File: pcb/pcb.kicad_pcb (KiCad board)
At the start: 6 copper layers, 186 parts, among them J1201 Conn_02x07_Top_Bottom, J1401 FPGA_JTAG, J201 USB_B_Mini, J301 Conn_02x05_Top_Bottom, J302 1658525-9, J601 DB15_Female_HighDensity, J801 10067847-001RLF, J901 FTSH-110-01-L-DV-007, U1402 S25FL127SABMFV101, U201 TPS54325PWPR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

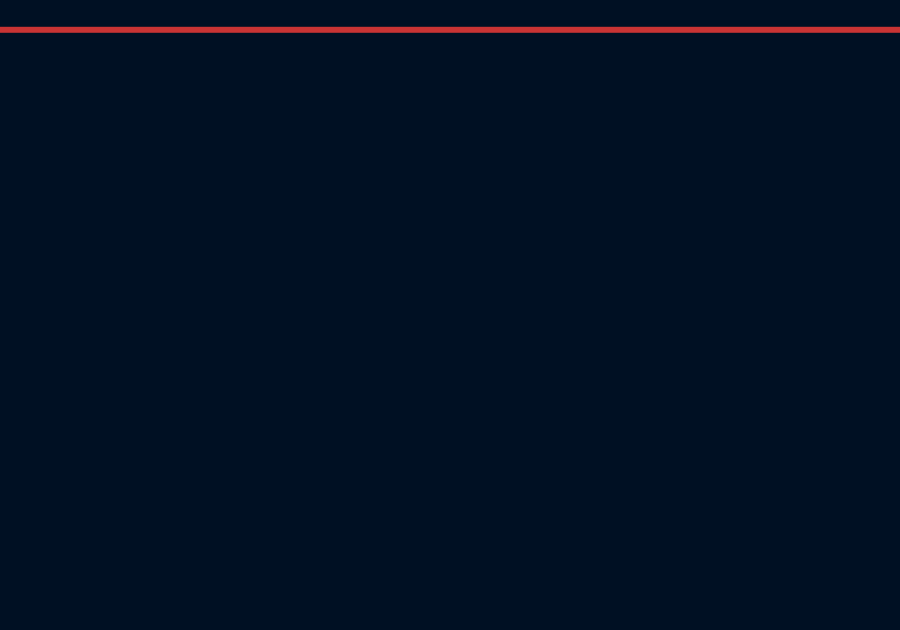
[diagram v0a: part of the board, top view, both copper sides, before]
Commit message: add correct vga resistors
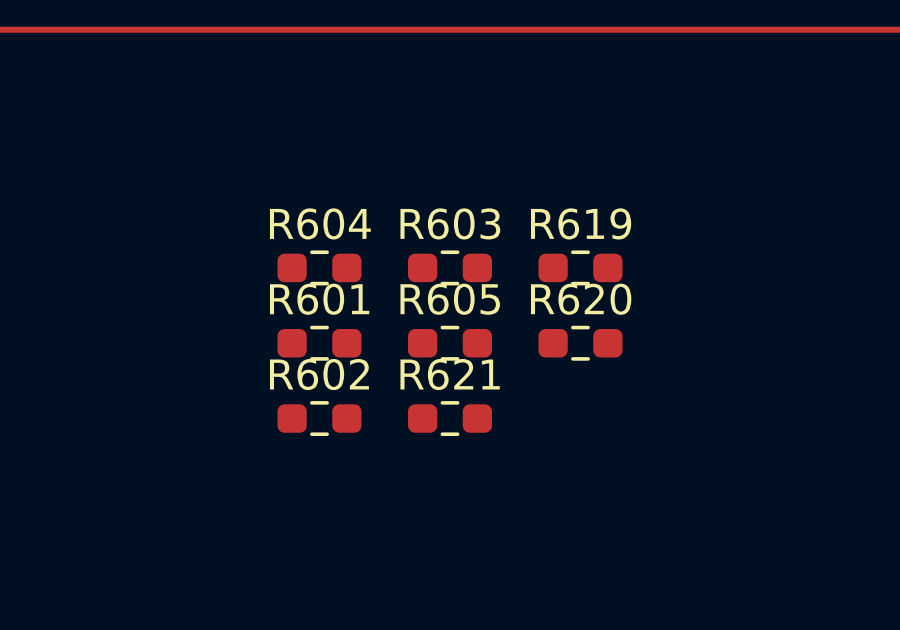
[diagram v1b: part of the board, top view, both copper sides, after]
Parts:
- added R601: 8760, Resistor_SMD:R_0603_1608Metric_Pad0.98x0.95mm_HandSolder, F.Cu at (141.5, 28.4)
- added R602: 4420, Resistor_SMD:R_0603_1608Metric_Pad0.98x0.95mm_HandSolder, F.Cu at (141.5, 31.0)
- added R603: 2200, Resistor_SMD:R_0603_1608Metric_Pad0.98x0.95mm_HandSolder, F.Cu at (145.8, 25.9)
- added R604: 1300, Resistor_SMD:R_0603_1608Metric_Pad0.98x0.95mm_HandSolder, F.Cu at (141.5, 25.9)
- added R605: 1100, Resistor_SMD:R_0603_1608Metric_Pad0.98x0.95mm_HandSolder, F.Cu at (145.8, 28.4)
- added R619: 1100, Resistor_SMD:R_0603_1608Metric_Pad0.98x0.95mm_HandSolder, F.Cu at (150.2, 25.9)
- added R620: 1100, Resistor_SMD:R_0603_1608Metric_Pad0.98x0.95mm_HandSolder, F.Cu at (150.2, 28.4)
- added R621: 1100, Resistor_SMD:R_0603_1608Metric_Pad0.98x0.95mm_HandSolder, F.Cu at (145.8, 31.0)
- R611, R616: value 550 -> 1100

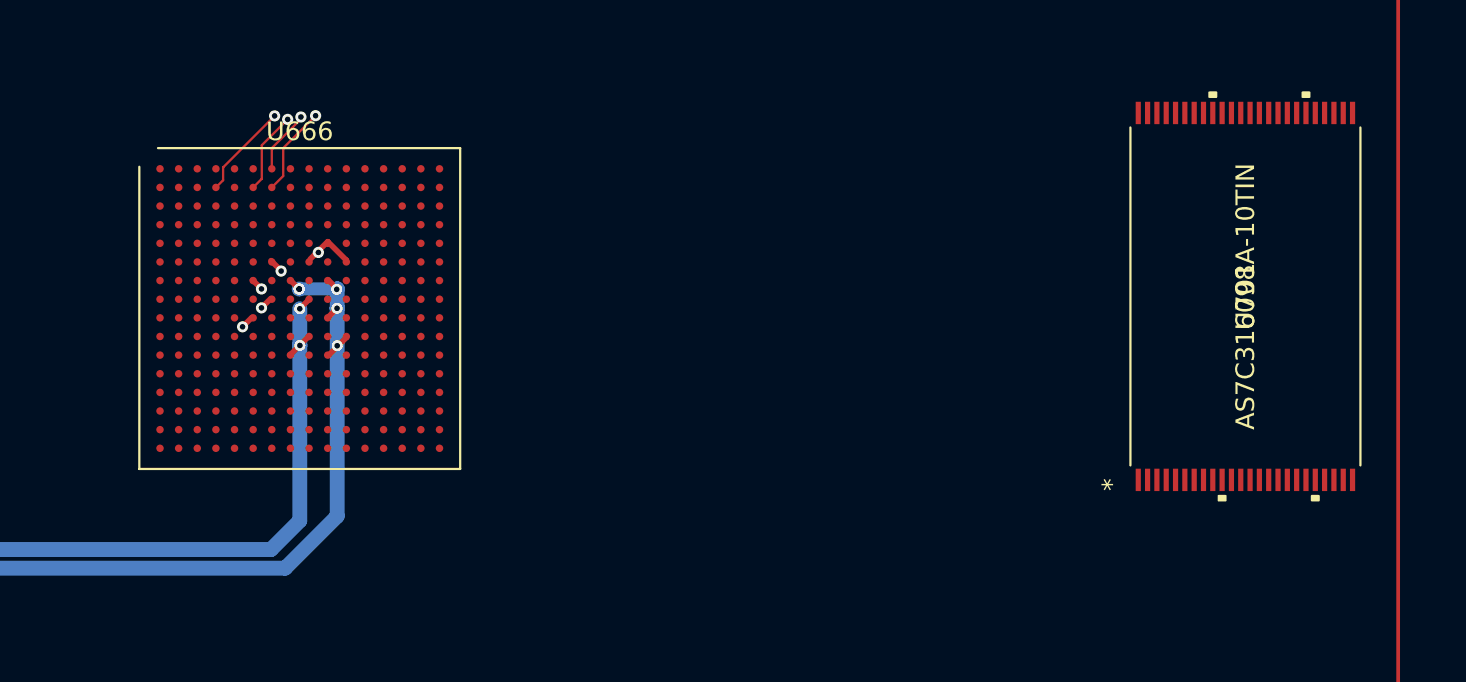
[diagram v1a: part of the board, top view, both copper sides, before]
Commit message: make lines between sram and fpga
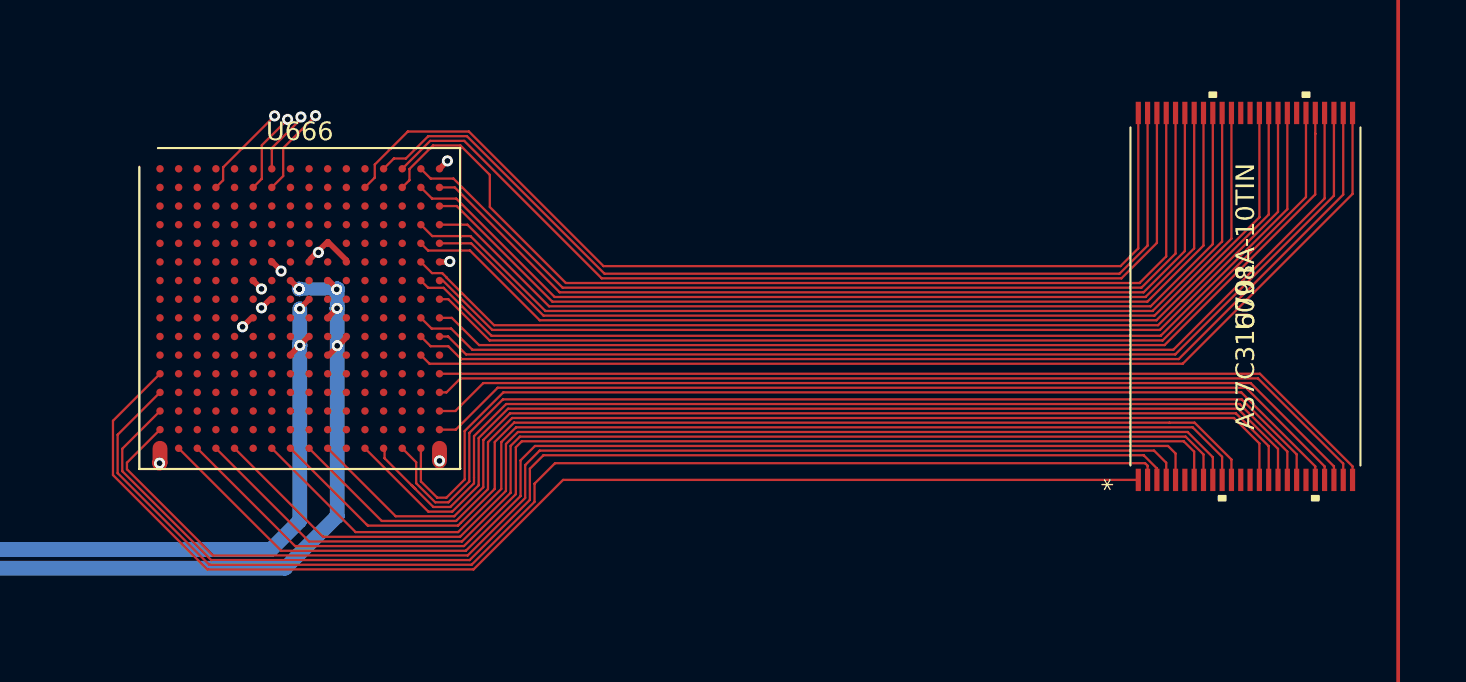
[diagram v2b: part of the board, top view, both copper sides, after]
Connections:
- U666 pad A13: vga_r2 -> SRAM_A6
- U666 pad A14: vga_r3 -> SRAM_A7
- U666 pad A15: vga_hsync -> SRAM_#OE
- U666 pad B12: vga_g4 -> SRAM_A5
- U666 pad B14: vga_r5 -> SRAM_A19
- U666 pad B15: unconnected-(U666-PadB15) -> SRAM_#LB
- U666 pad B16: unconnected-(U666-PadB16) -> SRAM_#UB
- U666 pad C16: vga_vsync -> SRAM_D15
- U666 pad D15: unconnected-(U666-PadD15) -> SRAM_D13
- U666 pad D16: unconnected-(U666-PadD16) -> SRAM_D14
- U666 pad E15: unconnected-(U666-PadE15) -> SRAM_D11
- U666 pad E16: unconnected-(U666-PadE16) -> SRAM_D12
- U666 pad F15: unconnected-(U666-PadF15) -> SRAM_D10
- U666 pad G15: unconnected-(U666-PadG15) -> SRAM_D8
- U666 pad G16: unconnected-(U666-PadG16) -> SRAM_D9
- U666 pad H16: unconnected-(U666-PadH16) -> SRAM_A8
- U666 pad J13: SRAM_A0 -> vga_r5
- U666 pad J14: SRAM_A1 -> unconnected-(U666-PadJ14)
- U666 pad J15: unconnected-(U666-PadJ15) -> SRAM_A10
- U666 pad J16: unconnected-(U666-PadJ16) -> SRAM_A9
- U666 pad K13: SRAM_A8 -> unconnected-(U666-PadK13)
- U666 pad K15: SRAM_A2 -> SRAM_A14
- U666 pad K16: SRAM_A3 -> SRAM_A11
- U666 pad L12: SRAM_A10 -> unconnected-(U666-PadL12)
- U666 pad L13: SRAM_A9 -> unconnected-(U666-PadL13)
- U666 pad L14: SRAM_A6 -> vga_r2
- U666 pad L15: SRAM_A4 -> SRAM_A16
- U666 pad M1: unconnected-(U666-PadM1) -> SRAM_A4
- U666 pad M12: SRAM_A11 -> unconnected-(U666-PadM12)
- U666 pad M14: SRAM_A7 -> vga_r3
- U666 pad M15: SRAM_A5 -> vga_g4
- U666 pad M6: SRAM_D14 -> unconnected-(U666-PadM6)
- U666 pad N1: unconnected-(U666-PadN1) -> SRAM_A3
- U666 pad N13: SRAM_D0 -> unconnected-(U666-PadN13)
- U666 pad N14: SRAM_D2 -> vga_hsync
- U666 pad N6: SRAM_D15 -> unconnected-(U666-PadN6)
- U666 pad N9: SRAM_D12 -> unconnected-(U666-PadN9)
- U666 pad P1: unconnected-(U666-PadP1) -> SRAM_A2
- U666 pad P10: SRAM_D4 -> unconnected-(U666-PadP10)
- U666 pad P11: SRAM_D5 -> unconnected-(U666-PadP11)
- U666 pad P13: SRAM_D1 -> unconnected-(U666-PadP13)
- U666 pad P14: SRAM_D3 -> unconnected-(U666-PadP14)
- U666 pad P15: SRAM_A14 -> unconnected-(U666-PadP15)
- U666 pad P8: SRAM_#CE -> unconnected-(U666-PadP8)
- U666 pad P9: SRAM_D13 -> vga_vsync
- U666 pad R1: unconnected-(U666-PadR1) -> SRAM_A1
- U666 pad R10: SRAM_D10 -> unconnected-(U666-PadR10)
- U666 pad R11: SRAM_D11 -> unconnected-(U666-PadR11)
- U666 pad R12: SRAM_D6 -> unconnected-(U666-PadR12)
- U666 pad R13: SRAM_D8 -> unconnected-(U666-PadR13)
- U666 pad R15: SRAM_A16 -> unconnected-(U666-PadR15)
- U666 pad R8: SRAM_#LB -> unconnected-(U666-PadR8)
- U666 pad T10: unconnected-(U666-PadT10) -> SRAM_D5
- U666 pad T12: SRAM_D7 -> SRAM_D6
- U666 pad T13: SRAM_D9 -> SRAM_D7
- U666 pad T14: SRAM_A18 -> SRAM_#WE
- U666 pad T15: SRAM_A19 -> SRAM_A0
- U666 pad T2: unconnected-(U666-PadT2) -> SRAM_A18
- U666 pad T3: unconnected-(U666-PadT3) -> SRAM_#CE
- U666 pad T4: unconnected-(U666-PadT4) -> SRAM_D0
- U666 pad T5: unconnected-(U666-PadT5) -> SRAM_D1
- U666 pad T7: SRAM_#OE -> SRAM_D2
- U666 pad T8: SRAM_#UB -> SRAM_D3
- U666 pad T9: SRAM_#WE -> SRAM_D4
- U701 pad 20: SRAM_A18 -> SRAM_A0
- U701 pad 22: SRAM_A16 -> SRAM_A15
- U701 pad 23: SRAM_A15 -> SRAM_A13
- U701 pad 24: SRAM_A14 -> SRAM_A12
- U701 pad 25: SRAM_A13 -> SRAM_A16
- U701 pad 26: SRAM_A12 -> SRAM_A14
- U701 pad 5: SRAM_A0 -> SRAM_A18
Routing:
- net SRAM_A3: track 0.00 -> 66.2 mm
- net SRAM_A2: track 0.00 -> 65.8 mm
- net SRAM_A4: track 0.00 -> 65.6 mm
- net SRAM_A1: track 0.00 -> 65.1 mm
- net SRAM_#CE: track 0.00 -> 61.2 mm
- net SRAM_A18: track 0.00 -> 60.8 mm
- net SRAM_D0: track 0.00 -> 60.6 mm
- net SRAM_D1: track 0.00 -> 60.1 mm
- net SRAM_D4: track 0.00 -> 58.9 mm
- net SRAM_D2: track 0.00 -> 58.6 mm
- net SRAM_D5: track 0.00 -> 58.3 mm
- net SRAM_A16: track 0.00 -> 58.3 mm
- net SRAM_A14: track 0.00 -> 58.0 mm
- net SRAM_D3: track 0.00 -> 57.9 mm
- net SRAM_A10: track 0.00 -> 57.2 mm
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- removed copper zone on In2.Cu, net +1V0
- removed copper zone on In2.Cu, net +1V8
